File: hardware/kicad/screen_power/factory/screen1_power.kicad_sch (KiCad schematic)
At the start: 18 parts, among them J103 SCREEN POWER 5V 3A, Q101 2N7002, Q102 2N7002, U102 SN74LVC1G14DBVR, U103 TPS25221DBVR, U104 TPS25810RVCR

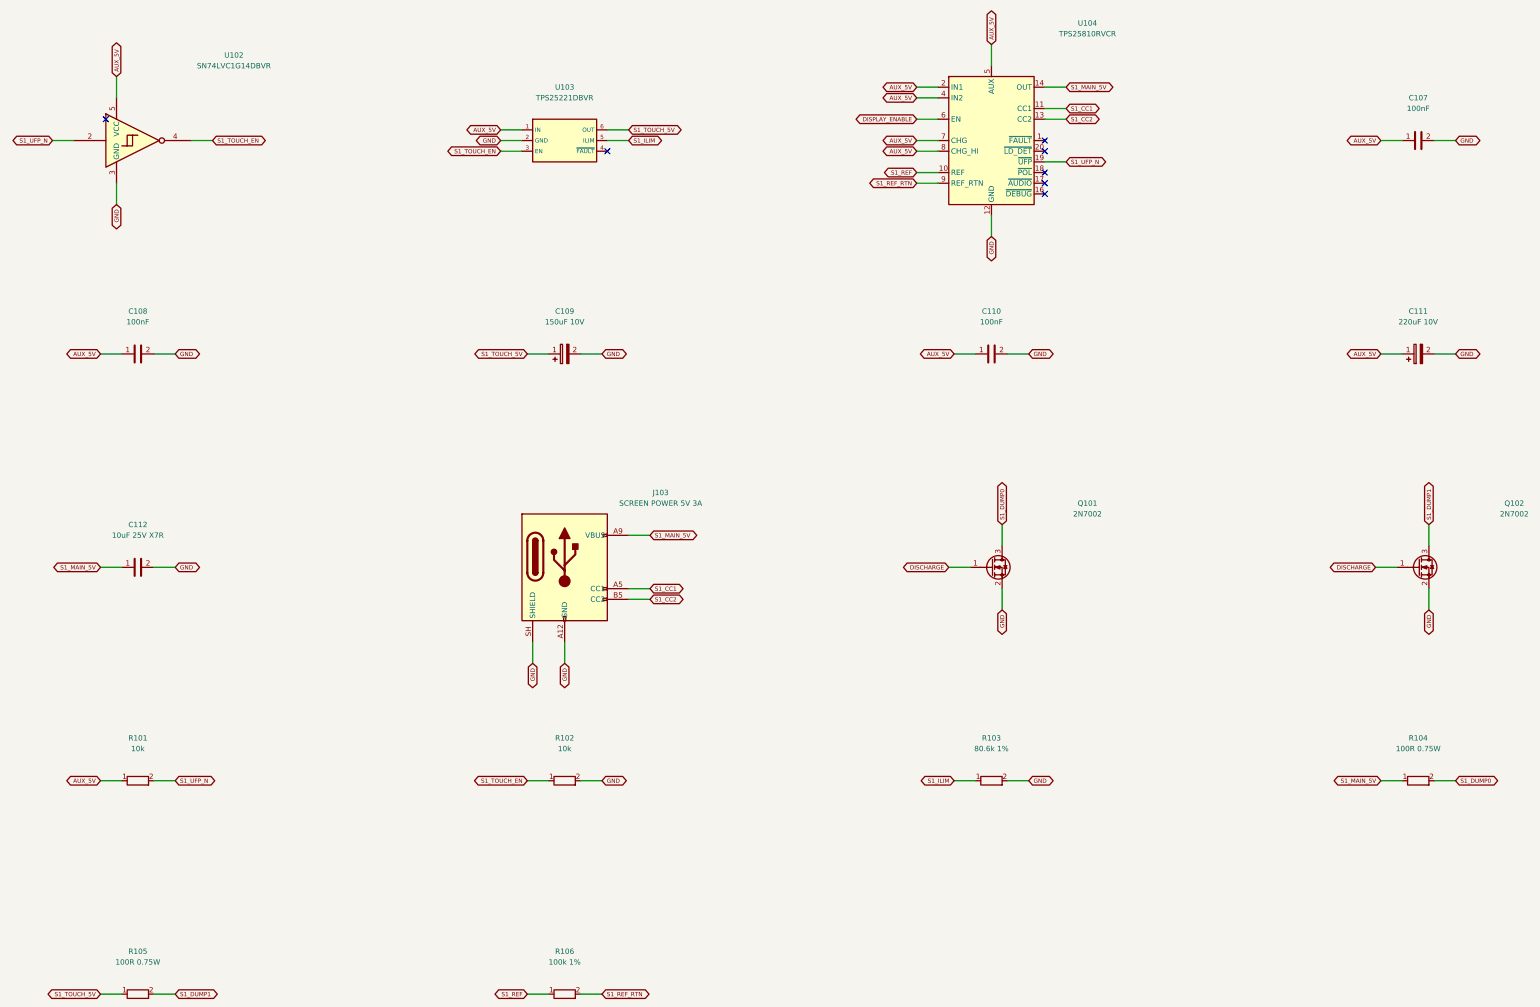
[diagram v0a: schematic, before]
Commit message: refactor(hardware): simplify and compact screen power boards
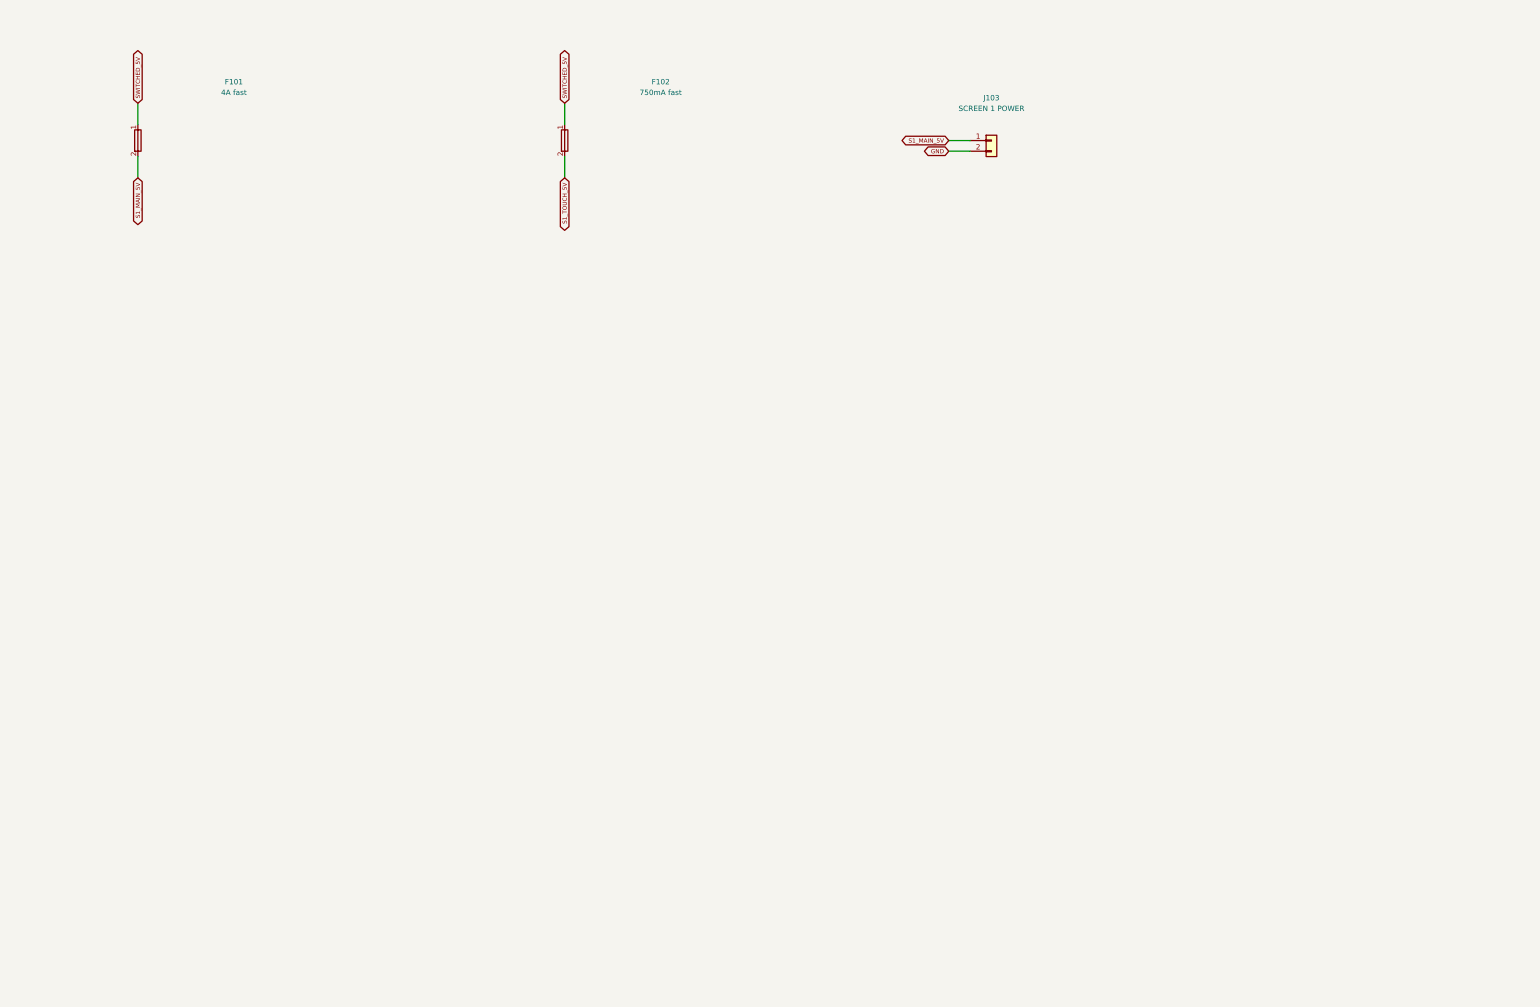
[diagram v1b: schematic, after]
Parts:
- removed C107, C108, C110: 100nF, Capacitor_SMD:C_0805_2012Metric, symbol screen_symbols:Device_C
- removed C109: 150uF 10V, Capacitor_THT:CP_Radial_D5.0mm_P2.00mm, symbol screen_symbols:Device_C_Polarized
- removed C111: 220uF 10V, Capacitor_THT:CP_Radial_D6.3mm_P2.50mm, symbol screen_symbols:Device_C_Polarized
- removed C112: 10uF 25V X7R, Capacitor_SMD:C_1210_3225Metric, symbol screen_symbols:Device_C
- removed Q101, Q102: 2N7002, Package_TO_SOT_SMD:SOT-23, symbol screen_symbols:Transistor_FET_2N7002
- removed R101, R102: 10k, Resistor_SMD:R_0805_2012Metric, symbol screen_symbols:Device_R
- removed R103: 80.6k 1%, Resistor_SMD:R_0805_2012Metric, symbol screen_symbols:Device_R
- removed R104, R105: 100R 0.75W, Resistor_SMD:R_2010_5025Metric, symbol screen_symbols:Device_R
- removed R106: 100k 1%, Resistor_SMD:R_0805_2012Metric, symbol screen_symbols:Device_R
- removed U102: SN74LVC1G14DBVR, Package_TO_SOT_SMD:SOT-23-5, symbol screen_symbols:74xGxx_SN74LVC1G14DBV
- removed U103: TPS25221DBVR, Package_TO_SOT_SMD:SOT-23-6, symbol screen_symbols:screen_power_TPS25221DBVR
- removed U104: TPS25810RVCR, Package_DFN_QFN:Texas_RVC0020A_WQFN-20-1EP_3x4mm_P0.5mm_EP1.6x2.6mm_ThermalVias, symbol screen_symbols:Interface_USB_TPS25810RVC
- added F101: 4A fast, screen_power:Fuse_Littelfuse_251_P12.70mm, symbol screen_symbols:Device_Fuse
- added F102: 750mA fast, screen_power:Fuse_Littelfuse_251_P12.70mm, symbol screen_symbols:Device_Fuse
- J103: value SCREEN POWER 5V 3A -> SCREEN 1 POWER; footprint Connector_USB:USB_C_Receptacle_GCT_USB4125-xx-x_6P_TopMnt_Horizontal -> Connector_JST:JST_VH_B2P-VH_1x02_P3.96mm_Vertical; symbol screen_symbols:Connector_USB_C_Receptacle_PowerOnly_6P -> screen_symbols:Connector_Generic_Conn_01x02; MPN USB4125-GF-A -> B2P-VH(LF)(SN)
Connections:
- net GND: now also J103.2 (Pin_2); no longer J103.A12 (GND), J103.B12 (GND), J103.SH (SHIELD)
- net S1_MAIN_5V: now also J103.1 (Pin_1), F101.2; no longer J103.A9 (VBUS), J103.B9 (VBUS)
- net S1_TOUCH_5V: now also F102.2
- removed net S1_CC1: J103.A5 (CC1)
- removed net S1_CC2: J103.B5 (CC2)
- new net SWITCHED_5V: F101.1, F102.1
- no-connect marks 7 -> 0
